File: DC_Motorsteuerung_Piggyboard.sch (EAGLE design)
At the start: 16 parts, among them X1 PFVERB10

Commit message: Piggyboard updated and finished !! (RGB-LED included)
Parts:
- removed X1: PFVERB10, Connector:PFVERB10
- added R7, R8: 90R, Resistor:R_0,4W
- added SV2: (no value), con-lstb:MA06-2
- D6: value Motor Fuse -> (none); device Test:LED3MM -> LED:RGB_LED_5MM
- R2, R5, R6: value 1,5 -> 1,5k
- R3: value 11k -> 1,5k
- R4: value 1,5 -> 160R
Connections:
- removed net N$8: S1.C, U$2.3, X1.9.1
- new net N$16: R4.1, SV2.6
- new net N$17: D6.BLUE, R7.2
- new net N$18: D6.GREEN, R8.2
- new net N$19: D6.RED, R4.2
- new net N$20: R6.1, SV2.5
- net GND: now also D6.CATHODE, SV2.11; no longer D6.C, X1.10.1
- net N$1: now also SV2.7; no longer X1.2.1
- net N$11: now also S1.C, SV2.12, U$2.3; no longer R6.1, X1.6.1
- net N$12: now also SV2.1; no longer X1.5.1
- net N$15: now also R7.1, SV2.2; no longer D6.A, R4.2
- net N$3: now also SV2.3; no longer X1.1.1
- net N$5: now also R8.1, SV2.4; no longer R4.1, X1.4.1
- net N$6: now also SV2.8; no longer X1.3.1
- net N$7: now also SV2.9; no longer X1.8.1
- net N$9: now also SV2.10; no longer X1.7.1
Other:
- note added: "Fehlerled (blue)"
- note added: "Fehlerled (green)"
- note added: "Fehlerled (rot)"
- note removed: "Motor Sicherung"
- moved on the sheet: D1, D2, D3, D4, D5, H1, R1, R2, R3, R4, R5, R6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

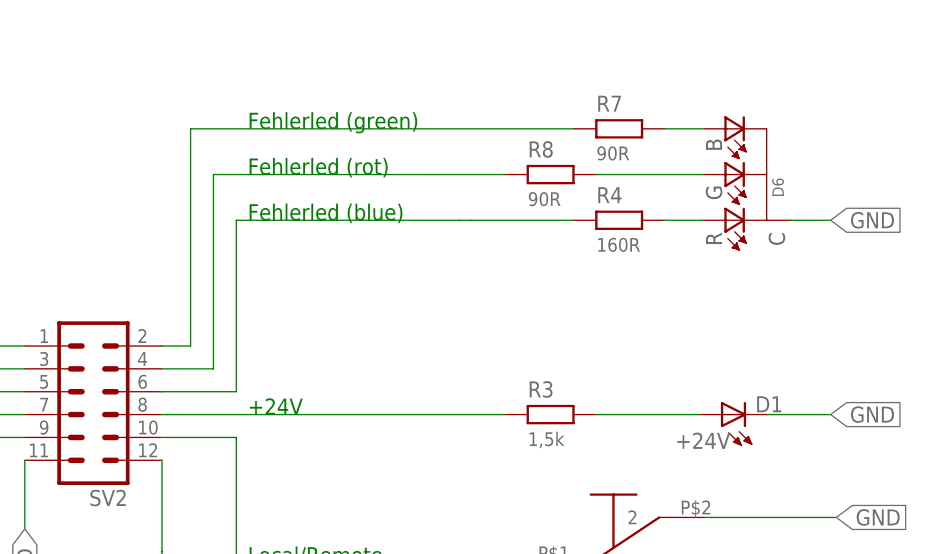
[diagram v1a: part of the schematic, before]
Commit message: Piggiboard updated (ERROR LED)
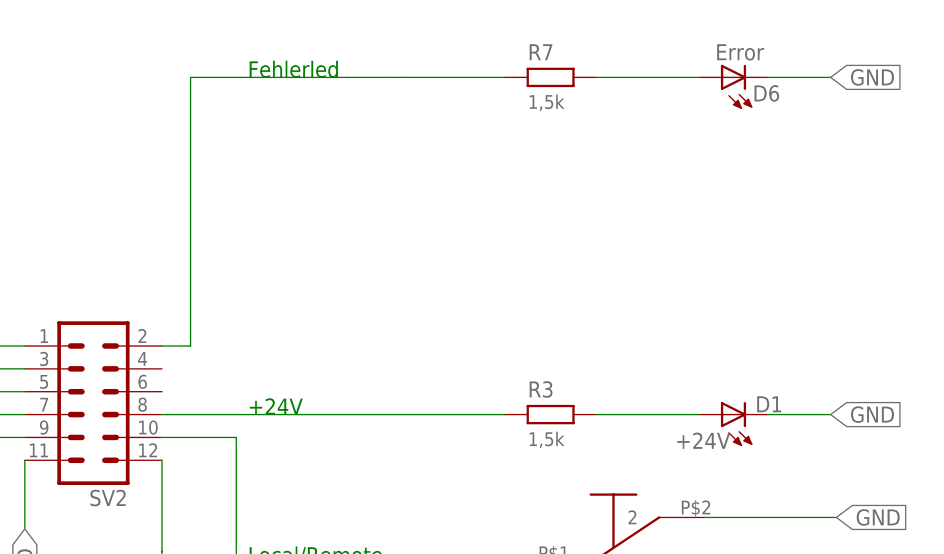
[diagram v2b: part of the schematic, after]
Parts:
- removed R4: 160R, Resistor:R_0,4W
- removed R8: 90R, Resistor:R_0,4W
- D6: value (none) -> Error; device LED:RGB_LED_5MM -> Test:LED3MM
- R7: value 90R -> 1,5k
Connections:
- removed net N$16: R4.1, SV2.6
- removed net N$17: D6.BLUE, R7.2
- removed net N$18: D6.GREEN, R8.2
- removed net N$19: D6.RED, R4.2
- net GND: now also D6.C; no longer D6.CATHODE
- net N$5: now also D6.A, R7.2; no longer R8.1, SV2.4
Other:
- note added: "Fehlerled"
- note removed: "Fehlerled (blue)"
- note removed: "Fehlerled (green)"
- note removed: "Fehlerled (rot)"
- moved on the sheet: R7
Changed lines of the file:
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@@
 <part name="H1" library="Holes" deviceset="MOUNT-HOLE" device="3.2" value="Das Loch 3,2 kilometer"/>
 <part name="U$2" library="Test" deviceset="UMSCHALTER_SINGLE_POLE" device=""/>
-<part name="D6" library="LED" deviceset="RGB_LED_5MM" device=""/>
 <part name="SV2" library="con-lstb" deviceset="MA06-2" device=""/>
-<part name="R4" library="Resistor" deviceset="R_0,4W" device="" value="160R"/>
-<part name="R8" library="Resistor" deviceset="R_0,4W" device="" value="90R"/>
-<part name="R7" library="Resistor" deviceset="R_0,4W" device="" value="90R"/>
+<part name="R7" library="Resistor" deviceset="R_0,4W" device="" value="1,5k"/>
+<part name="D6" library="Test" deviceset="LED3MM" device="" value="Error"/>
 </parts>
 <sheets>
@@
 <text x="152.4" y="161.925" size="1.778" layer="91" font="vector">Endschalter A</text>
 <text x="152.4" y="136.525" size="1.778" layer="91" font="vector">Endschalter B</text>
-<text x="207.01" y="163.195" size="1.778" layer="91" font="vector">Fehlerled (rot)</text>
 <text x="197.485" y="113.03" size="1.778" layer="91" font="vector" rot="R90">+5V</text>
-<text x="207.01" y="158.115" size="1.778" layer="91" font="vector">Fehlerled (blue)</text>
-<text x="207.01" y="168.275" size="1.778" layer="91" font="vector">Fehlerled (green)</text>
+<text x="207.01" y="173.99" size="1.778" layer="91" font="vector">Fehlerled</text>
 </plain>
 <instances>
@@
 <instance part="H1" gate="G$1" x="86.36" y="59.055"/>
 <instance part="U$2" gate="G$1" x="250.19" y="120.015"/>
-<instance part="D6" gate="G$1" x="260.985" y="163.195" rot="R90"/>
 <instance part="SV2" gate="1" x="189.865" y="136.525" rot="R180"/>
-<instance part="R4" gate="G$1" x="248.285" y="158.115"/>
-<instance part="R8" gate="G$1" x="240.665" y="163.195"/>
-<instance part="R7" gate="G$1" x="248.285" y="168.275"/>
+<instance part="R7" gate="G$1" x="240.665" y="173.99"/>
+<instance part="D6" gate="G$1" x="259.715" y="173.99" smashed="yes" rot="R90">
+<attribute name="NAME" x="266.192" y="173.101" size="1.778" layer="95" rot="R180"/>
+<attribute name="VALUE" x="258.953" y="175.895" size="1.778" layer="96"/>
+</instance>
 </instances>
 <busses>
@@
 </segment>
 <segment>
-<pinref part="D6" gate="G$1" pin="CATHODE"/>
-<wire x1="267.335" y1="158.115" x2="271.78" y2="158.115" width="0.1524" layer="91"/>
-<label x="271.78" y="158.115" size="1.778" layer="95" font="vector" xref="yes"/>
+<wire x1="264.795" y1="173.99" x2="271.78" y2="173.99" width="0.1524" layer="91"/>
+<label x="271.78" y="173.99" size="1.778" layer="95" font="vector" xref="yes"/>
+<pinref part="D6" gate="G$1" pin="C"/>
 </segment>
 </net>
@@
 </segment>
 </net>
-<net name="N$5" class="0">
-<segment>
-<wire x1="203.2" y1="163.195" x2="226.695" y2="163.195" width="0.1524" layer="91"/>
-<wire x1="226.695" y1="163.195" x2="227.965" y2="163.195" width="0.1524" layer="91"/>
-<pinref part="R8" gate="G$1" pin="1"/>
-<wire x1="227.965" y1="163.195" x2="235.585" y2="163.195" width="0.1524" layer="91"/>
-<pinref part="SV2" gate="1" pin="4"/>
-<wire x1="197.485" y1="141.605" x2="203.2" y2="141.605" width="0.1524" layer="91"/>
-<wire x1="203.2" y1="141.605" x2="203.2" y2="163.195" width="0.1524" layer="91"/>
-</segment>
-</net>
 <net name="N$6" class="0">
 <segment>
@@
 <segment>
 <pinref part="R7" gate="G$1" pin="1"/>
-<wire x1="243.205" y1="168.275" x2="224.155" y2="168.275" width="0.1524" layer="91"/>
-<wire x1="224.155" y1="168.275" x2="222.885" y2="168.275" width="0.1524" layer="91"/>
-<wire x1="222.885" y1="168.275" x2="200.66" y2="168.275" width="0.1524" layer="91"/>
+<wire x1="235.585" y1="173.99" x2="224.155" y2="173.99" width="0.1524" layer="91"/>
+<wire x1="224.155" y1="173.99" x2="222.885" y2="173.99" width="0.1524" layer="91"/>
+<wire x1="222.885" y1="173.99" x2="200.66" y2="173.99" width="0.1524" layer="91"/>
 <pinref part="SV2" gate="1" pin="2"/>
 <wire x1="197.485" y1="144.145" x2="200.66" y2="144.145" width="0.1524" layer="91"/>
-<wire x1="200.66" y1="144.145" x2="200.66" y2="168.275" width="0.1524" layer="91"/>
-</segment>
-</net>
-<net name="N$16" class="0">
-<segment>
-<pinref part="R4" gate="G$1" pin="1"/>
-<wire x1="243.205" y1="158.115" x2="231.775" y2="158.115" width="0.1524" layer="91"/>
-<wire x1="231.775" y1="158.115" x2="230.505" y2="158.115" width="0.1524" layer="91"/>
-<wire x1="230.505" y1="158.115" x2="205.74" y2="158.115" width="0.1524" layer="91"/>
-<pinref part="SV2" gate="1" pin="6"/>
-<wire x1="197.485" y1="139.065" x2="205.74" y2="139.065" width="0.1524" layer="91"/>
-<wire x1="205.74" y1="139.065" x2="205.74" y2="158.115" width="0.1524" layer="91"/>
-</segment>
-</net>
-<net name="N$17" class="0">
-<segment>
-<pinref part="R7" gate="G$1" pin="2"/>
-<wire x1="253.365" y1="168.275" x2="257.683" y2="168.275" width="0.1524" layer="91"/>
-<pinref part="D6" gate="G$1" pin="BLUE"/>
-</segment>
-</net>
-<net name="N$18" class="0">
-<segment>
-<pinref part="R8" gate="G$1" pin="2"/>
-<pinref part="D6" gate="G$1" pin="GREEN"/>
-<wire x1="257.683" y1="163.195" x2="245.745" y2="163.195" width="0.1524" layer="91"/>
-</segment>
-</net>
-<net name="N$19" class="0">
-<segment>
-<pinref part="R4" gate="G$1" pin="2"/>
-<wire x1="253.365" y1="158.115" x2="257.683" y2="158.115" width="0.1524" layer="91"/>
-<pinref part="D6" gate="G$1" pin="RED"/>
+<wire x1="200.66" y1="144.145" x2="200.66" y2="173.99" width="0.1524" layer="91"/>
 </segment>
 </net>
@@
 </segment>
 </net>
+<net name="N$5" class="0">
+<segment>
+<pinref part="R7" gate="G$1" pin="2"/>
+<pinref part="D6" gate="G$1" pin="A"/>
+<wire x1="245.745" y1="173.99" x2="257.175" y2="173.99" width="0.1524" layer="91"/>
+</segment>
+</net>
